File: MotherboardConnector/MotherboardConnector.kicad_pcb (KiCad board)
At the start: 2 copper layers, 67 x 73.5 mm, 13 parts, among them J1 Amphenol 10035388-102LF PCB e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, J2 1862262, J3 1862262, J4 1862262, J5 1862262, U1 NE12S0A0V10PNF

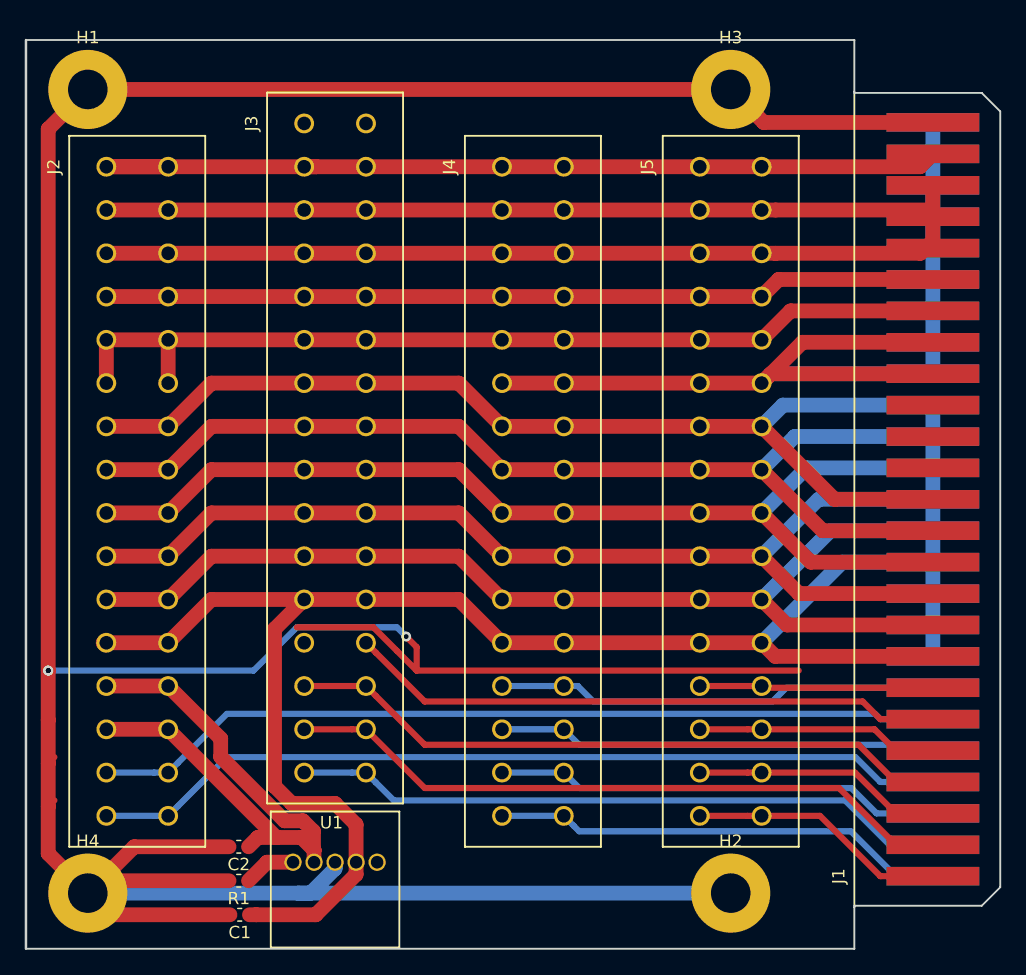
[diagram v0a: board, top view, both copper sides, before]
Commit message: completed motherboard connector PCB
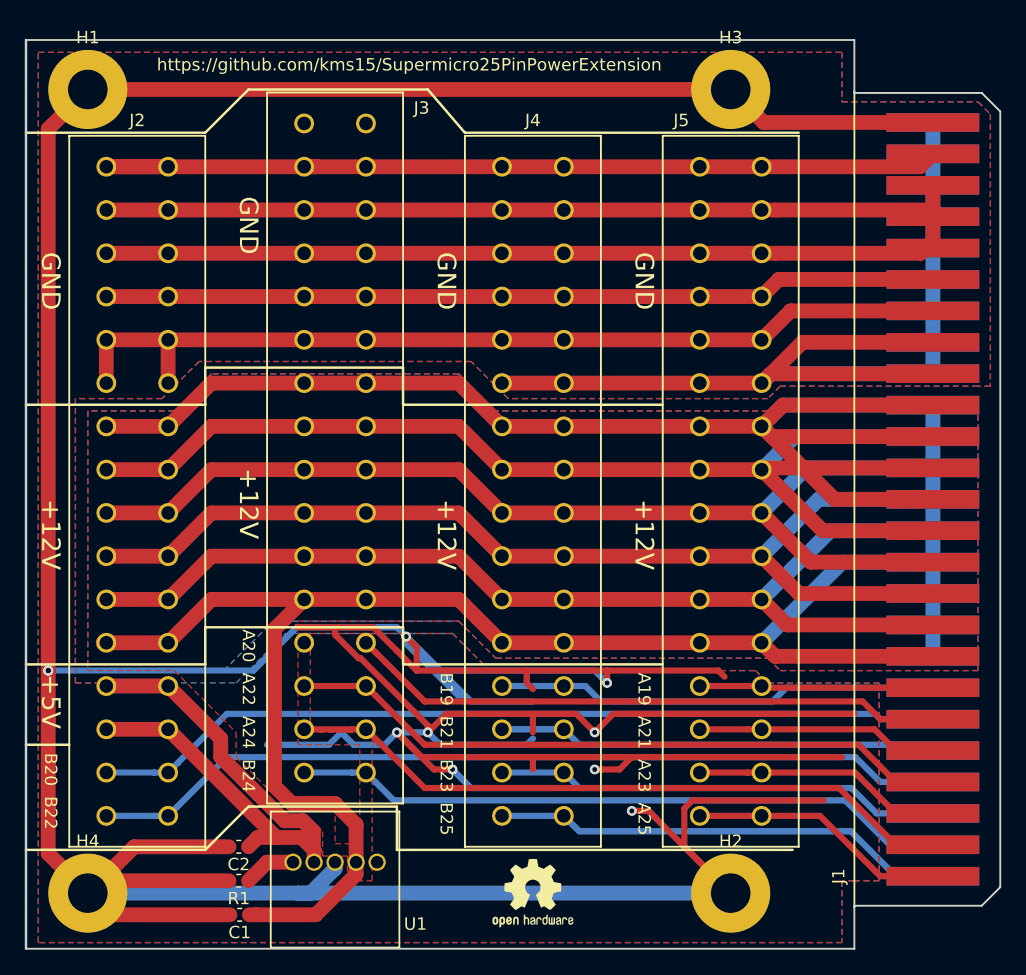
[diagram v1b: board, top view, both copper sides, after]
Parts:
- added REF**: OSHW-Logo2_7.3x6mm_SilkScreen, Symbol:OSHW-Logo2_7.3x6mm_SilkScreen, F.Cu at (174.0, 119.0)
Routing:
- net GND: track 746.2 -> 942.0 mm, vias 3 -> 10
- net +12V: track 579.3 -> 622.0 mm
- added copper zone on B.Cu, net +12V
- added copper zone on F.Cu, net +12V
- added copper zone on B.Cu, net GND
- added copper zone on F.Cu, net GND
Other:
- board text added: "+12V"
- board text added: "+5V"
- board text added: "A19"
- board text added: "A20"
- board text added: "A21"
- board text added: "A22"
- board text added: "A23"
- board text added: "A24"
- board text added: "A25"
- board text added: "B19"
- board text added: "B20"
- board text added: "B21"
- board text added: "B22"
- board text added: "B23"
- board text added: "B24"
- board text added: "B25"
- board text added: "GND"
- board text added: "https://github.com/kms15/Supermicro25PinPowerExtension"
